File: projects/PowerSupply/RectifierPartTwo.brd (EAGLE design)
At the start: 90 x 65 mm, 13 parts, among them K1 G2R2, X1 LINE-IN, X2 T2-PRI, X3 T2-SEC, X4 R2-OUT

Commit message: feat: rectifier part two modified
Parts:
- C2: value 2200µF -> 4700µF
- F2: value 6.3AT -> 4A
- X4: value R2-OUT -> (none); device con-wago-508:W237-133 -> con-wago-508:W237-132
- moved C2 33.6 mm to (40.0, 45.0), turned to 45 degrees
- moved D1 29.2 mm to (70.0, 30.0), turned to 90 degrees
- moved X3 16.0 mm to (49.0, 5.00)
- moved X4 15.0 mm to (45.0, 60.0)
- moved C1 13.6 mm to (57.0, 45.0), turned to 45 degrees
- moved F2 8.00 mm to (40.0, 23.0)
- moved F3 7.81 mm to (57.0, 23.0), turned to 90 degrees
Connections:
- removed net GND: C1.-, C2.+, X3.5, X3.6, X4.2
- removed net N$20: C1.+, D1.+VDC, X4.3
- removed net N$21: C2.-, D1.-VDC, X4.1
- new net N$1: D1.VAC2, X3.2
- new net N$4: F3.1, X3.6
- net N$2: now also D1.VAC1, F3.2, X3.1; no longer D1.VAC2, X3.2, X3.4
- net N$3: now also D1.+VDC; no longer F3.2, X3.1
- net N$5: now also C1.+, C2.+, X4.2; no longer D1.VAC1
- net N$6: now also C1.-, C2.-, D1.-VDC, X4.1; no longer F3.1, X3.3
- net PE: now also X3.3, X3.4, X3.5
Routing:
- net GND: track 80.8 -> 0.00 mm
- net N$1: track 0.00 -> 42.5 mm
- net N$21: track 32.7 -> 0.00 mm
- net N$20: track 31.6 -> 0.00 mm
- net N$6: track 21.4 -> 44.4 mm
- net N$2: track 80.9 -> 58.8 mm
- net PE: track 5.08 -> 15.2 mm
- net N$4: track 0.00 -> 9.33 mm
- net N$5: track 37.4 -> 46.6 mm
- net N$3: track 24.9 -> 32.3 mm
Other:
- board size 90 x 65 mm -> 75 x 65 mm

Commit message: feat: rectifier parts modified
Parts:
- F1: value 1.6AT -> 1AT
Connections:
- new net N$7: X3.3, X3.4
- net N$1: now also F3.2, X3.6; no longer X3.2
- net N$2: now also X3.2; no longer F3.2
- net N$4: now also X3.5; no longer X3.6
- net PE: no longer X3.3, X3.4, X3.5
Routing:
- net PE: track 15.2 -> 5.08 mm
- net N$7: track 0.00 -> 5.08 mm
- net N$4: track 9.33 -> 7.54 mm
- net N$1: track 42.5 -> 43.5 mm
- net N$2: track 58.8 -> 58.3 mm
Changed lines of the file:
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@@
 <setting verticaltext="up"/>
 </settings>
-<grid distance="19.6850394" unitdist="mil" unit="mil" style="lines" multiple="1" display="yes" altdistance="0.5" altunitdist="mm" altunit="mm"/>
+<grid distance="0.5" unitdist="mm" unit="mm" style="lines" multiple="1" display="yes" altdistance="0.5" altunitdist="mm" altunit="mm"/>
 <layers>
 <layer number="1" name="Top" color="4" fill="1" visible="yes" active="yes"/>
@@
 <attribute name="VALUE" x="66" y="47" size="1.27" layer="27" rot="R90"/>
 </element>
-<element name="F1" library="fuse" library_urn="urn:adsk.eagle:library:233" package="SH22,5A" package3d_urn="urn:adsk.eagle:package:14070/1" value="1.6AT" x="23" y="59" smashed="yes">
+<element name="F1" library="fuse" library_urn="urn:adsk.eagle:library:233" package="SH22,5A" package3d_urn="urn:adsk.eagle:package:14070/1" value="1AT" x="23" y="59" smashed="yes">
 <attribute name="MF" value="" x="48.4" y="27.25" size="1.778" layer="27" display="off"/>
 <attribute name="MPN" value="0031.7701.11" x="48.4" y="27.25" size="1.778" layer="27" display="off"/>
@@
 <contactref element="X1" pad="3"/>
 <wire x1="4.365" y1="37.46" x2="4.365" y2="42.54" width="1.27" layer="16"/>
-<contactref element="X3" pad="3"/>
-<contactref element="X3" pad="4"/>
-<contactref element="X3" pad="5"/>
-<wire x1="56.62" y1="4.365" x2="51.54" y2="4.365" width="3.81" layer="16"/>
-<wire x1="51.54" y1="4.365" x2="46.46" y2="4.365" width="3.81" layer="16"/>
-<wire x1="4.365" y1="37.46" x2="46.46" y2="4.365" width="0" layer="19" extent="1-1"/>
 </signal>
 <signal name="+230VAC">
@@
 <wire x1="11" y1="19" x2="23.634" y2="19" width="1.27" layer="16"/>
 </signal>
-<signal name="N$1">
-<contactref element="X3" pad="2"/>
-<contactref element="D1" pad="VAC2"/>
-<wire x1="69.95" y1="35" x2="41.38" y2="6.43" width="3.81" layer="1"/>
-<wire x1="41.38" y1="6.43" x2="41.38" y2="4.365" width="3.81" layer="1"/>
-</signal>
 <signal name="N$2">
 <contactref element="X3" pad="1"/>
 <contactref element="D1" pad="VAC1"/>
-<contactref element="F3" pad="2"/>
-<wire x1="69.95" y1="27.5" x2="63.1978" y2="34.2522" width="3.81" layer="16"/>
-<wire x1="63.1978" y1="34.2522" x2="57" y2="34.2522" width="3.81" layer="16"/>
-<wire x1="57" y1="34.2522" x2="51.7522" y2="34.2522" width="3.81" layer="16"/>
-<wire x1="51.7522" y1="34.2522" x2="34.5" y2="17" width="3.81" layer="16"/>
-<wire x1="34.5" y1="17" x2="34.5" y2="6.165" width="3.81" layer="16"/>
+<contactref element="X3" pad="2"/>
 <wire x1="36.3" y1="4.365" x2="34.5" y2="6.165" width="3.81" layer="16"/>
-</signal>
-<signal name="N$4">
-<contactref element="X3" pad="6"/>
-<contactref element="F3" pad="1"/>
-<wire x1="61.7" y1="4.365" x2="61.7" y2="7.0478" width="3.81" layer="16"/>
-<wire x1="61.7" y1="7.0478" x2="57" y2="11.7478" width="3.81" layer="16"/>
+<wire x1="34.5" y1="6.165" x2="34.5" y2="17" width="3.81" layer="16"/>
+<wire x1="34.5" y1="17" x2="45" y2="27.5" width="3.81" layer="16"/>
+<wire x1="45" y1="27.5" x2="69.95" y2="27.5" width="3.81" layer="16"/>
+<wire x1="36.3" y1="4.365" x2="41.38" y2="4.365" width="3.81" layer="16"/>
 </signal>
 <signal name="N$3">
 <contactref element="D1" pad="+VDC"/>
 <contactref element="F2" pad="1"/>
-<wire x1="40" y1="11.7478" x2="44.7478" y2="11.7478" width="2.032" layer="16"/>
-<wire x1="44.7478" y1="11.7478" x2="50.5" y2="17.5" width="2.032" layer="16"/>
-<wire x1="50.5" y1="17.5" x2="69.95" y2="17.5" width="2.032" layer="16"/>
+<wire x1="40" y1="11.7478" x2="46.2478" y2="11.7478" width="2.032" layer="16"/>
+<wire x1="46.2478" y1="11.7478" x2="52" y2="17.5" width="2.032" layer="16"/>
+<wire x1="52" y1="17.5" x2="69.95" y2="17.5" width="2.032" layer="16"/>
 </signal>
 <signal name="N$5">
@@
 <wire x1="64.755925" y1="47.694075" x2="69.95" y2="42.5" width="2.032" layer="16"/>
 </signal>
+<signal name="N$7">
+<contactref element="X3" pad="3"/>
+<contactref element="X3" pad="4"/>
+<wire x1="46.46" y1="4.365" x2="51.54" y2="4.365" width="3.81" layer="16"/>
+</signal>
+<signal name="N$4">
+<contactref element="X3" pad="5"/>
+<contactref element="F3" pad="1"/>
+<wire x1="56.62" y1="4.365" x2="56.62" y2="11.3678" width="3.81" layer="16"/>
+<wire x1="56.62" y1="11.3678" x2="57" y2="11.7478" width="3.81" layer="16"/>
+</signal>
+<signal name="N$1">
+<contactref element="X3" pad="6"/>
+<contactref element="F3" pad="2"/>
+<contactref element="D1" pad="VAC2"/>
+<wire x1="57" y1="34.2522" x2="61.7" y2="29.5522" width="3.81" layer="1"/>
+<wire x1="61.7" y1="29.5522" x2="61.7" y2="26.75" width="3.81" layer="1"/>
+<wire x1="61.7" y1="22.5" x2="61.7" y2="4.365" width="3.81" layer="1"/>
+<wire x1="61.7" y1="22.5" x2="61.7" y2="26.75" width="3.81" layer="1"/>
+<wire x1="61.7" y1="26.75" x2="69.95" y2="35" width="3.81" layer="1"/>
+</signal>
 </signals>

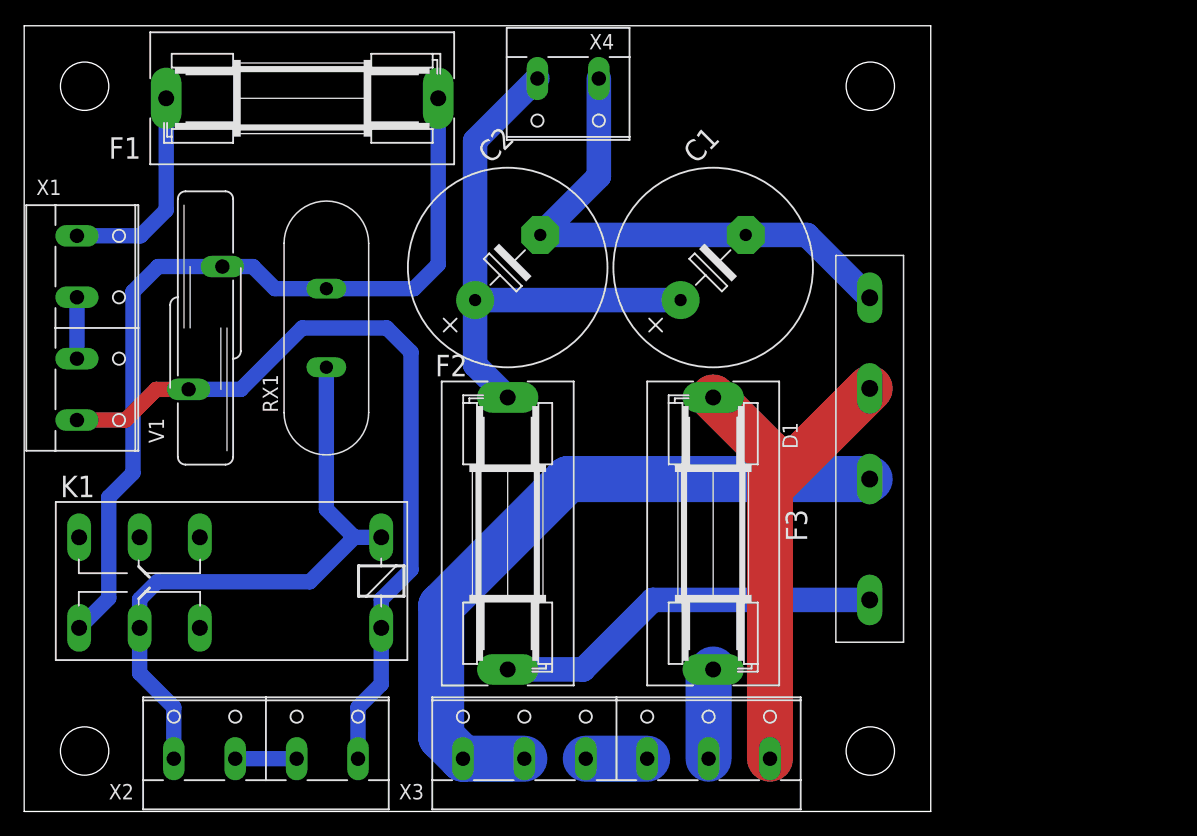
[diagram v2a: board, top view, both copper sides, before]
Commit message: feat: rectifier part modified
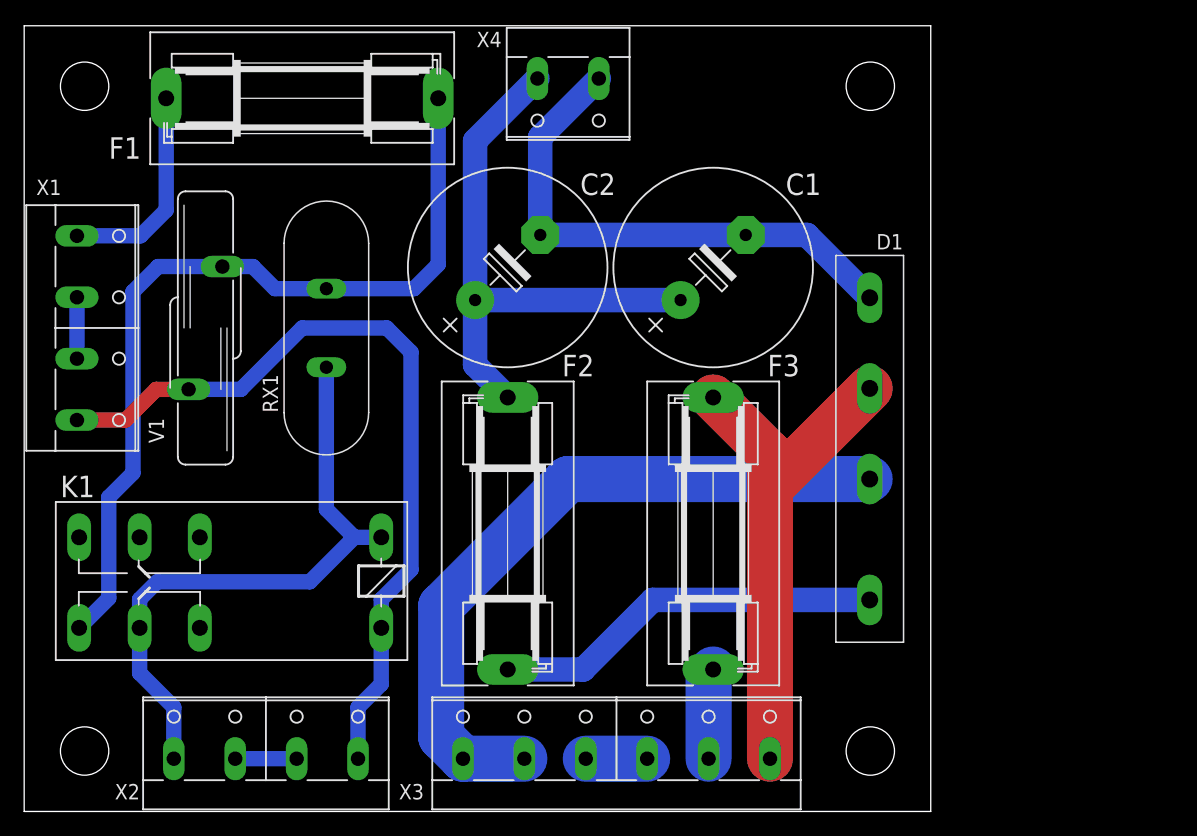
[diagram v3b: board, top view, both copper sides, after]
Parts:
- X4: value (none) -> 30V
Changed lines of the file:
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@@
 <elements>
 <element name="C1" library="rcl" library_urn="urn:adsk.eagle:library:334" package="E7,5-16" package3d_urn="urn:adsk.eagle:package:23382/2" value="2200µF" x="57" y="45" smashed="yes" rot="R45">
-<attribute name="NAME" x="55.585784375" y="53.48528125" size="1.778" layer="25" ratio="10" rot="R45"/>
+<attribute name="NAME" x="63" y="51" size="1.778" layer="25" ratio="10"/>
 <attribute name="POPULARITY" value="4" x="87.53286875" y="62.960509375" size="1.778" layer="27" rot="R45" display="off"/>
 <attribute name="SPICEPREFIX" value="C" x="87.53286875" y="62.960509375" size="1.778" layer="27" rot="R45" display="off"/>
@@
 </element>
 <element name="C2" library="rcl" library_urn="urn:adsk.eagle:library:334" package="E7,5-16" package3d_urn="urn:adsk.eagle:package:23382/2" value="4700µF" x="40" y="45" smashed="yes" rot="R45">
-<attribute name="NAME" x="38.585784375" y="53.48528125" size="1.778" layer="25" ratio="10" rot="R45"/>
+<attribute name="NAME" x="46" y="51" size="1.778" layer="25" ratio="10"/>
 <attribute name="POPULARITY" value="4" x="84.901278125" y="77.328921875" size="1.778" layer="27" rot="R45" display="off"/>
 <attribute name="SPICEPREFIX" value="C" x="84.901278125" y="77.328921875" size="1.778" layer="27" rot="R45" display="off"/>
@@
 </element>
 <element name="D1" library="bb84" package="B..C" value="B40C5000-3300A" x="70" y="30" smashed="yes" rot="R90">
-<attribute name="NAME" x="64" y="30" size="1.27" layer="25" rot="R90"/>
-<attribute name="VALUE" x="66" y="47" size="1.27" layer="27" rot="R90"/>
+<attribute name="NAME" x="70.5" y="46.5" size="1.27" layer="25"/>
+<attribute name="VALUE" x="72.5" y="14.5" size="1.27" layer="27" rot="R90"/>
 </element>
 <element name="F1" library="fuse" library_urn="urn:adsk.eagle:library:233" package="SH22,5A" package3d_urn="urn:adsk.eagle:package:14070/1" value="1AT" x="23" y="59" smashed="yes">
@@
 <attribute name="MF" value="" x="71.75" y="75.07" size="1.778" layer="27" rot="R90" display="off"/>
 <attribute name="MPN" value="0031.7701.11" x="71.75" y="75.07" size="1.778" layer="27" rot="R90" display="off"/>
-<attribute name="NAME" x="34" y="36" size="1.778" layer="25" ratio="10"/>
+<attribute name="NAME" x="44.5" y="36" size="1.778" layer="25" ratio="10"/>
 <attribute name="OC_FARNELL" value="unknown" x="71.75" y="75.07" size="1.778" layer="27" rot="R90" display="off"/>
 <attribute name="OC_NEWARK" value="04F1224" x="71.75" y="75.07" size="1.778" layer="27" rot="R90" display="off"/>
@@
 <attribute name="MF" value="" x="102.72" y="48.4" size="1.778" layer="27" rot="R90" display="off"/>
 <attribute name="MPN" value="0031.7701.11" x="102.72" y="48.4" size="1.778" layer="27" rot="R90" display="off"/>
-<attribute name="NAME" x="63" y="25" size="1.778" layer="25" ratio="10" rot="R270"/>
+<attribute name="NAME" x="61.5" y="36" size="1.778" layer="25" ratio="10"/>
 <attribute name="OC_FARNELL" value="unknown" x="102.72" y="48.4" size="1.778" layer="27" rot="R90" display="off"/>
 <attribute name="OC_NEWARK" value="04F1224" x="102.72" y="48.4" size="1.778" layer="27" rot="R90" display="off"/>
@@
 <attribute name="MF" value="" x="65.72" y="-67.39" size="1.778" layer="27" display="off"/>
 <attribute name="MPN" value="" x="65.72" y="-67.39" size="1.778" layer="27" display="off"/>
-<attribute name="NAME" x="7" y="1" size="1.27" layer="25" ratio="10"/>
+<attribute name="NAME" x="7.5" y="1" size="1.27" layer="25" ratio="10"/>
 <attribute name="OC_FARNELL" value="unknown" x="65.72" y="-67.39" size="1.778" layer="27" display="off"/>
 <attribute name="OC_NEWARK" value="unknown" x="65.72" y="-67.39" size="1.778" layer="27" display="off"/>
@@
 <attribute name="VALUE" x="57" y="1" size="1.27" layer="27" ratio="10"/>
 </element>
-<element name="X4" library="con-wago-508" library_urn="urn:adsk.eagle:library:196" package="W237-132" package3d_urn="urn:adsk.eagle:package:10734/1" value="" x="45" y="60" smashed="yes" rot="R180">
+<element name="X4" library="con-wago-508" library_urn="urn:adsk.eagle:library:196" package="W237-132" package3d_urn="urn:adsk.eagle:package:10734/1" value="30V" x="45" y="60" smashed="yes" rot="R180">
 <attribute name="MF" value="" x="45" y="60" size="1.778" layer="27" rot="R180" display="off"/>
 <attribute name="MPN" value="" x="45" y="60" size="1.778" layer="27" rot="R180" display="off"/>
-<attribute name="NAME" x="48.81" y="64.318" size="1.27" layer="25" ratio="10" rot="R180"/>
+<attribute name="NAME" x="39.5" y="64.5" size="1.27" layer="25" ratio="10" rot="R180"/>
 <attribute name="OC_FARNELL" value="unknown" x="45" y="60" size="1.778" layer="27" rot="R180" display="off"/>
 <attribute name="OC_NEWARK" value="unknown" x="45" y="60" size="1.778" layer="27" rot="R180" display="off"/>
 <attribute name="POPULARITY" value="10" x="45" y="60" size="1.778" layer="27" rot="R180" display="off"/>
-<attribute name="VALUE" x="48.81" y="66.985" size="1.27" layer="27" ratio="10" rot="R180"/>
+<attribute name="VALUE" x="49.5" y="64.5" size="1.27" layer="27" ratio="10" rot="R180"/>
 </element>
 </elements>
@@
 <contactref element="D1" pad="-VDC"/>
 <wire x1="59.694075" y1="47.694075" x2="42.694075" y2="47.694075" width="2.032" layer="16"/>
-<wire x1="42.694075" y1="47.694075" x2="47.54" y2="52.54" width="2.032" layer="16"/>
-<wire x1="47.54" y1="52.54" x2="47.54" y2="60.635" width="2.032" layer="16"/>
 <wire x1="59.694075" y1="47.694075" x2="64.755925" y2="47.694075" width="2.032" layer="16"/>
 <wire x1="64.755925" y1="47.694075" x2="69.95" y2="42.5" width="2.032" layer="16"/>
+<wire x1="42.694075" y1="47.694075" x2="42.694075" y2="55.789075" width="2.032" layer="16"/>
+<wire x1="42.694075" y1="55.789075" x2="47.54" y2="60.635" width="2.032" layer="16"/>
 </signal>
 <signal name="N$7">

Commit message: feat: rectifier part modified
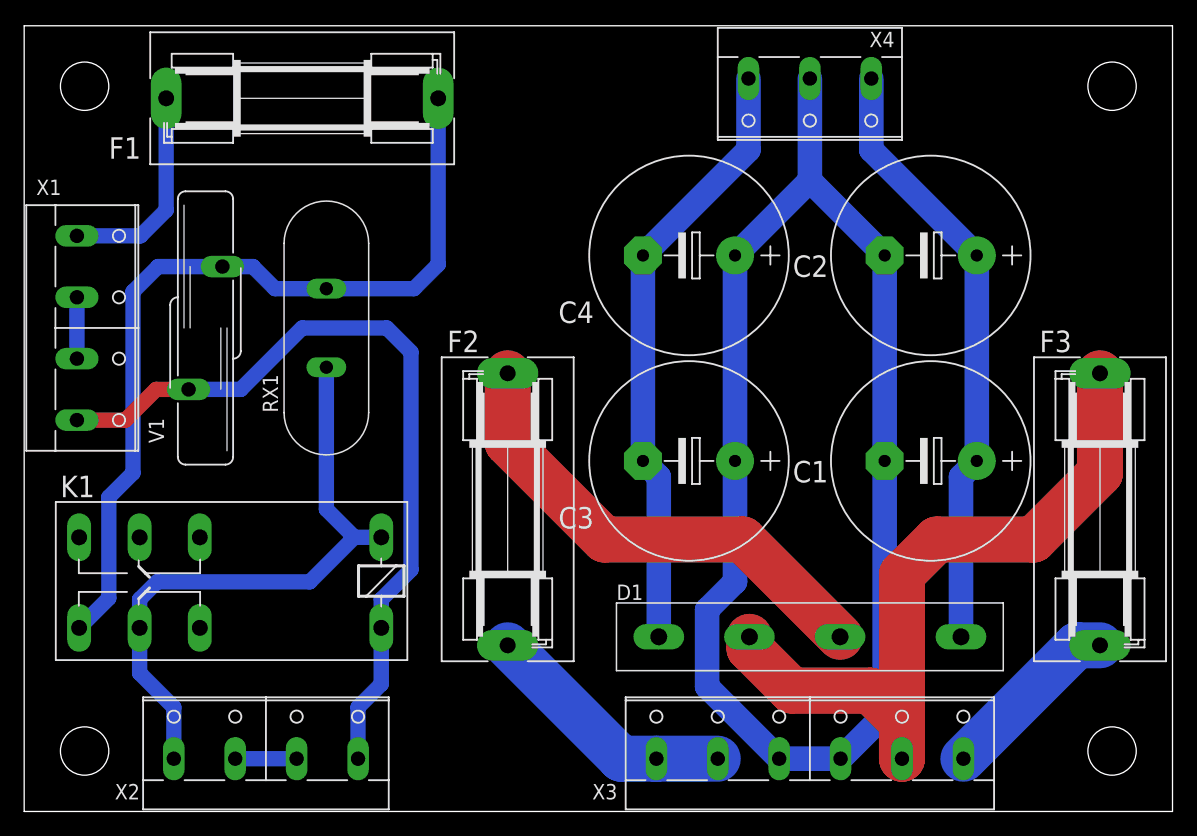
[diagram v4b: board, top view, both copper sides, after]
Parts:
- added C3, C4: 2200µF, rcl:E7,5-16
- C2: value 4700µF -> 2200µF
- F2: value 4A -> 6.3AT
- X4: value 30V -> (none); device con-wago-508:W237-132 -> con-wago-508:W237-133
- moved C2 35.0 mm to (75.0, 46.0), turned to 180 degrees
- moved F3 32.1 mm to (89.0, 25.0)
- moved C1 24.1 mm to (75.0, 29.0), turned to 180 degrees
- moved X4 20.0 mm to (65.0, 60.0)
- moved D1 16.3 mm to (65.0, 14.5), turned to 180 degrees
- moved X3 16.0 mm to (65.0, 5.00)
- moved F2 2.00 mm to (40.0, 25.0)
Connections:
- removed net N$7: X3.3, X3.4
- new net N$8: D1.VAC1, F2.2
- net N$1: now also X3.5; no longer X3.6
- net N$2: now also F2.1; no longer D1.VAC1
- net N$3: now also C3.-, C4.-, D1.-VDC, X4.3; no longer D1.+VDC, F2.1
- net N$4: now also X3.6; no longer X3.5
- net N$5: now also D1.+VDC, X4.1; no longer F2.2, X4.2
- net N$6: now also C3.+, C4.+, X3.3, X3.4, X4.2; no longer D1.-VDC, X4.1
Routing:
- net N$6: track 44.4 -> 119.2 mm
- net N$8: track 0.00 -> 39.9 mm
- net N$2: track 58.3 -> 21.3 mm
- net N$1: track 43.5 -> 62.5 mm
- net N$3: track 32.3 -> 50.3 mm
- net N$4: track 7.54 -> 15.2 mm
- net N$7: track 5.08 -> 0.00 mm
- net N$5: track 46.6 -> 50.3 mm
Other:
- board size 75 x 65 mm -> 95 x 65 mm
